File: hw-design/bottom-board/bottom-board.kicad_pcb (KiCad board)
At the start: 2 copper layers, 172 x 140.5 mm, 256 parts, among them J1 JACK_TRS_6PINS, J2 JACK_TRS_6PINS, J3 JACK_TRS_6PINS, J4 JACK_TRS_6PINS, J5 JACK_TRS_6PINS, J6 RJ45_LEDS, J7 Conn_02x50_Odd_Even, J8 Conn_02x50_Odd_Even, K1 IM06TS, K2 IM06TS, P1 USB_B, P2 USB_A, P3 DIN_5, P4 DIN_5, P5 BARREL_JACK, P6 HMI_POWER, P8 HMI_DATA, P9 SERIAL_DEBUG, Q1 2N7002, Q10 2N7002, Q12 2N7002, Q13 2N7002, Q14 BSS84, Q15 BSS84, Q2 2N7002, Q3 J112, Q4 J112, Q5 J112, Q6 J112, Q7 2N7002, Q8 2N7002, Q9 2N7002, SW1 SW_PUSH, U1 MURATA 5V, U10 RT9701, U11 6N137S, U12 ISL83491, U13 AP2120N-3.3, U2 LD1117S50TR_SOT223, U3 CS4245, U4 AT24CS08-STUM, U6 LM4562, U7 LM4562, U8 LM4562, U9 LM4811

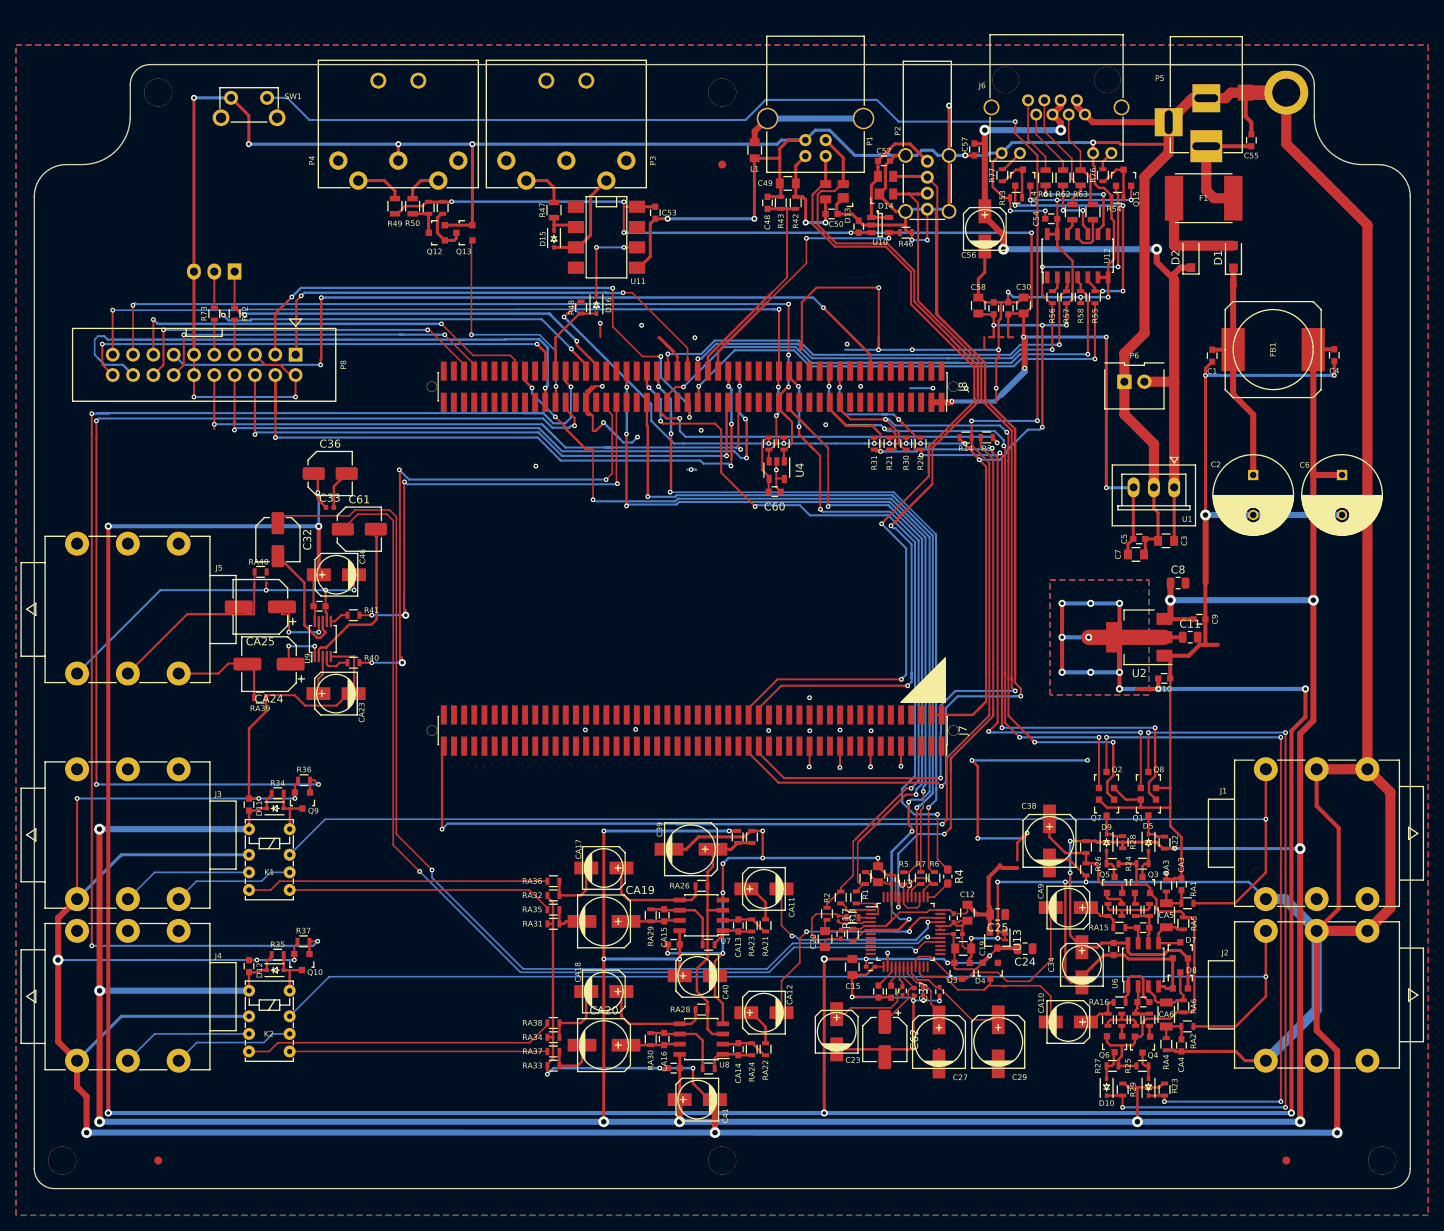
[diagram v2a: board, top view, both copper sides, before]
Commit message: Changed capacitor posistion & changed relay footprint
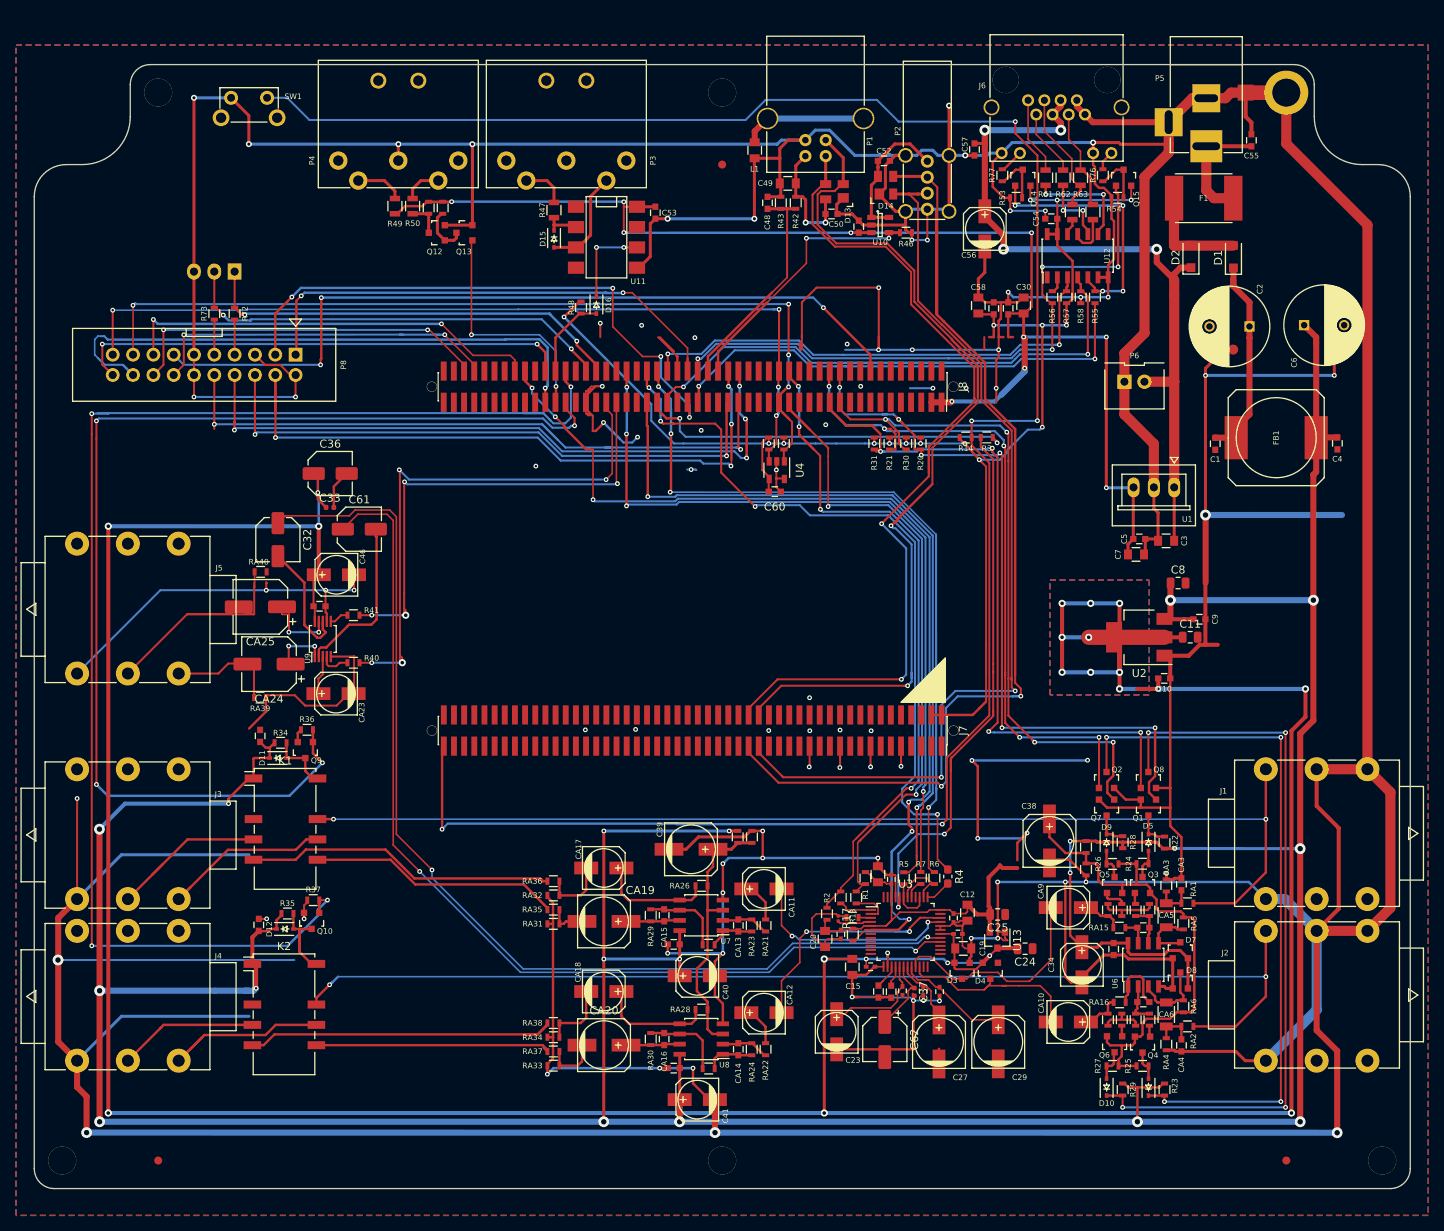
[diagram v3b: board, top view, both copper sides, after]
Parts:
- K1, K2: footprint footprints:Relay_DPDT_IMXXTS -> footprints:Relay_DPDT_Omron_G6S-2F-good_pinout
- moved C6 19.3 mm to (218.8, 52.1), turned to 0 degrees
- moved C2 18.6 mm to (212.0, 52.3), turned to 180 degrees
- moved C4 11.0 mm to (223.0, 66.9)
- moved C1 11.0 mm to (207.7, 67.0)
- moved FB1 11.0 mm to (215.3, 66.2)
- moved C44 8.70 mm to (88.3, 103.5)
- moved D11 6.31 mm to (90.6, 106.2)
- moved Q9 6.31 mm to (94.0, 105.3)
- moved R34 6.31 mm to (90.9, 104.3)
- moved R36 6.31 mm to (94.2, 102.7)
- moved K2 5.34 mm to (91.3, 138.3)
- moved D12 5.29 mm to (91.4, 127.6)
- moved C45 5.29 mm to (88.1, 127.1)
- moved Q10 5.29 mm to (94.7, 126.6)
- moved R35 5.29 mm to (91.7, 125.7)
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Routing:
- net GNDA: track 1634.4 -> 1596.5 mm, vias 88 -> 86
- net +12VA: track 519.5 -> 531.6 mm, vias 17 -> 19
- net RIGHT_AUDIO_OUTPUT_TIP: track 15.3 -> 23.2 mm
- net LEFT_AUDIO_OUTPUT_TIP: track 15.3 -> 22.6 mm
- net Net-(D12-Pad2): track 6.90 -> 12.5 mm
- net LEFT_AUDIO_INPUT: track 147.4 -> 142.1 mm, vias 1 -> 2
- net LEFT_TRUE_BYPASS: track 140.9 -> 145.5 mm
- net Net-(C1-Pad1): track 30.3 -> 26.1 mm
- net LEFT_AUDIO_OUTPUT_RING: track 16.5 -> 20.6 mm
- net RIGHT_TRUE_BYPASS: track 170.8 -> 174.6 mm
- net RIGHT_AUDIO_INPUT: track 142.9 -> 139.4 mm, vias 1 -> 2
- net Net-(K2-Pad4): track 38.9 -> 41.9 mm
- net Net-(K2-Pad5): track 32.2 -> 30.0 mm
- net Net-(K1-Pad4): track 37.8 -> 39.3 mm
- net Net-(K1-Pad5): track 33.3 -> 34.8 mm
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
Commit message: added logo's and updated gerber files
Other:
- board text added: "MOD Devices GmbH http://moddevices.com [DU-ELE-001] MOD Duo - Bottom Board Rev.: 2019.04.15"
- board text removed: "MOD Devices GmbH http://moddevices.com MOD Duo - Bottom Board Rev.: 2019.03.28"
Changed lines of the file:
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@@
   )
   (layers
-    (0 F.Cu signal)
-    (31 B.Cu signal)
+    (0 F.Cu signal hide)
+    (31 B.Cu signal hide)
     (32 B.Adhes user)
     (33 F.Adhes user)
@@
     (effects (font (size 1 1) (thickness 0.15)) (justify left mirror))
   )
-  (gr_text "MOD Devices GmbH\nhttp://moddevices.com\n\nMOD Duo - Bottom Board\nRev.: 2019.03.28" (at 208.71434 141.54912) (layer B.SilkS)
-    (effects (font (size 1.5 1.5) (thickness 0.3)) (justify left mirror))
+  (gr_text "MOD Devices GmbH\nhttp://moddevices.com\n\n[DU-ELE-001]\nMOD Duo - Bottom Board\nRev.: 2019.04.15" (at 208.71434 141.54912) (layer B.SilkS)
+    (effects (font (size 2 2) (thickness 0.4)) (justify left mirror))
   )
   (segment (start 209.931 46.49724) (end 209.93354 46.49978) (width 0.762) (layer F.Cu) (net 1) (status 30))

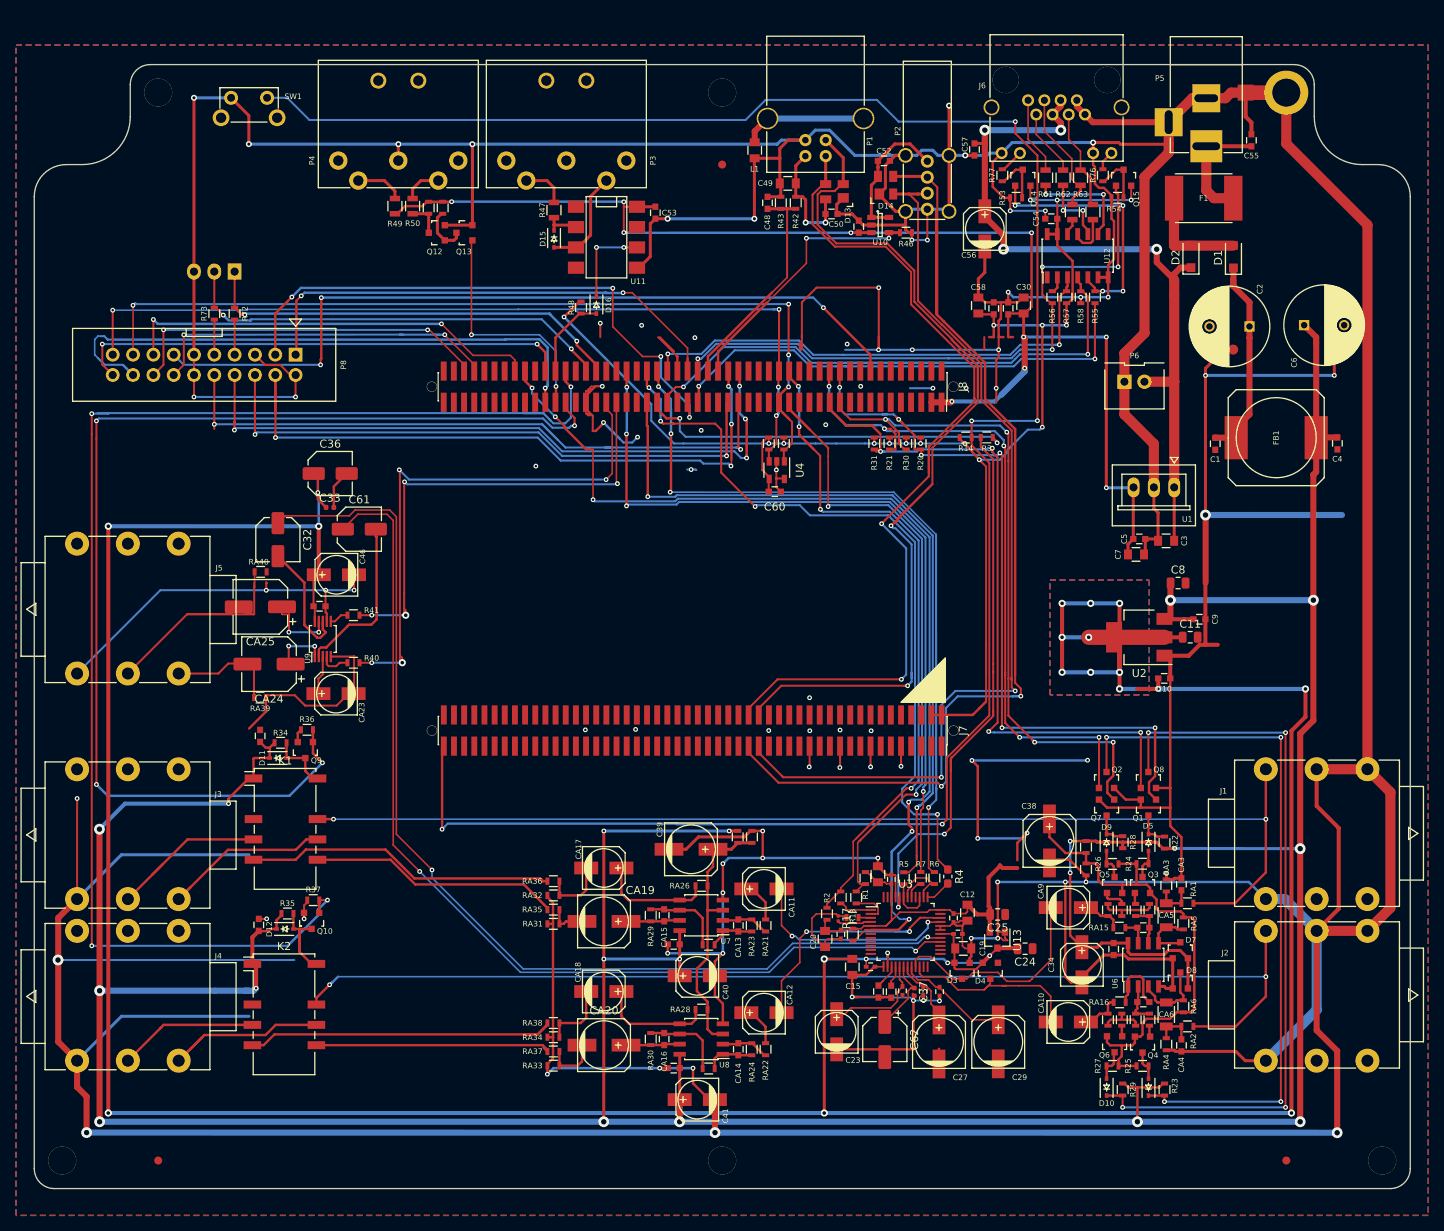
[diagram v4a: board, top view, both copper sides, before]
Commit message: updated footprints and MPN's
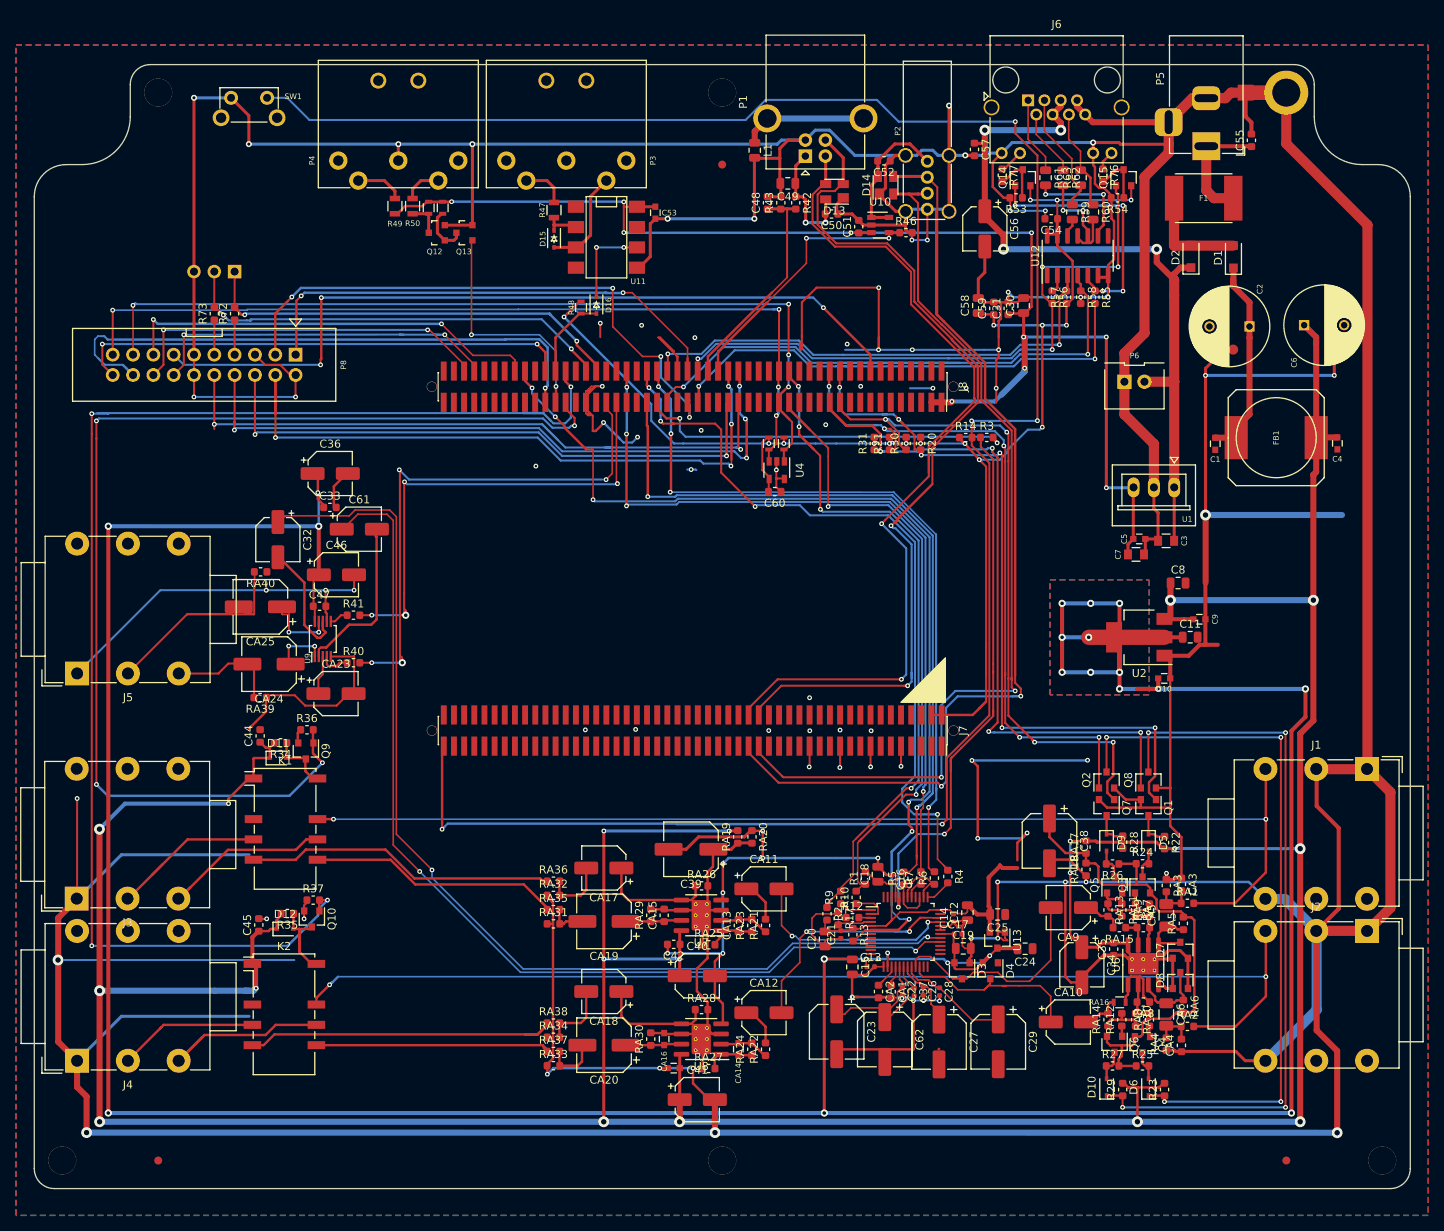
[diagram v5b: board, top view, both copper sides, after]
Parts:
- C12, C15, C18, C19, C20, C30, C49, C58, L1: footprint Capacitors_SMD:C_0805 -> Capacitor_SMD:C_0805_2012Metric
- C13, C14, C16, C17, C21, C22, C26, C28: footprint Capacitors_SMD:C_0402 -> Capacitor_SMD:C_0402_1005Metric
- C23: footprint Capacitors_SMD:c_elec_5x5.3 -> Capacitor_SMD:CP_Elec_6.3x5.3
- C27, C29, C38, C39: footprint Capacitors_SMD:c_elec_6.3x5.3 -> Capacitor_SMD:CP_Elec_6.3x5.3
- C31, C35, C42, C44, C45, C47, C48, C50, C51, C52, C54, C55, C57, C59, C60, CA1, CA13, CA15, CA2, CA3, CA4, CA7, CA8: footprint Capacitors_SMD:C_0603 -> Capacitor_SMD:C_0603_1608Metric
- C32, C36, C61: footprint Capacitor_SMD:C_Elec_5x5.4 -> Capacitor_SMD:CP_Elec_5x5.3
- C33: footprint Capacitor_SMD:C_0402_1005Metric -> Capacitor_SMD:C_0603_1608Metric
- C34, C40, C41, C46, C56, CA10, CA11, CA12, CA17, CA18, CA23, CA9: footprint Capacitors_SMD:c_elec_5x5.3 -> Capacitor_SMD:CP_Elec_5x5.3
- C62: footprint Capacitor_SMD:CP_Elec_5x5.3 -> Capacitor_SMD:CP_Elec_6.3x5.3
- CA19, CA20: footprint Capacitors_SMD:c_elec_6.3x7.7 -> Capacitor_SMD:CP_Elec_6.3x7.7
- CA5, CA6: footprint Capacitors_SMD:C_1206 -> Capacitor_SMD:C_1206_3216Metric
- D10, D11, D12, D5, D6, D9: footprint Diodes_SMD:SOD-323 -> Diode_SMD:D_SOD-323
- D13, D14: footprint Housings_SOT-23_SOT-143_TSOT-6:SOT-143 -> Package_TO_SOT_SMD:SOT-143
- D3, D4, D7, D8, Q1, Q10, Q14, Q15, Q2, Q3, Q4, Q5, Q6, Q7, Q8, Q9: footprint Housings_SOT-23_SOT-143_TSOT-6:SOT-23 -> Package_TO_SOT_SMD:SOT-23
- J1, J2, J3, J4, J5: footprint Connect:NMJ6HCD2 -> Connector_Audio:Jack_3.5mm_Neutrik_NMJ6HCD2_Horizontal
- J6: footprint Connect:RJHSE538X -> Connector_RJ:RJ45_Amphenol_RJHSE538X
- J7, J8: footprint footprints-local:Pin_Header_Straight_2x50_Pitch1.27mm_SMD -> footprints:Pin_Header_Straight_2x50_Pitch1.27mm_SMD
- P1: footprint Connect:USB_B -> Connector_USB:USB_B_OST_USB-B1HSxx_Horizontal
- P5: footprint Connect:BARREL_JACK -> Connector_BarrelJack:BarrelJack_Horizontal
- P9: footprint Pin_Headers:Pin_Header_Straight_1x03 -> Connector_PinHeader_2.54mm:PinHeader_1x03_P2.54mm_Vertical
- R1, R10, R12, R13, R14, R2, R20, R21, R22, R23, R24, R25, R26, R27, R28, R29, R3, R30, R31, R34, R35, R36, R37, R40, R41, R42, R43, R46, R5, R53, R54, R55, R56, R57, R58, R6, R7, R72, R73, R76, R77, R9, RA1, RA10, RA11, RA12, RA13, RA14, RA15, RA17, RA18, RA19, RA2, RA20, RA21, RA22, RA23, RA24, RA25, RA26, RA27, RA28, RA29, RA3, RA30, RA31, RA32, RA33, RA34, RA35, RA36, RA37, RA38, RA39, RA4, RA40, RA5, RA6, RA7, RA8, RA9: footprint Resistors_SMD:R_0603 -> Resistor_SMD:R_0603_1608Metric
- R17: footprint Resistor_SMD:R_0201_0603Metric -> Resistor_SMD:R_0603_1608Metric
- R4: footprint Resistor_SMD:R_0603_1608Metric_Pad1.05x0.95mm_HandSolder -> Resistor_SMD:R_0603_1608Metric
- R59, R60, R61, R62, R63: footprint Resistors_SMD:R_0805 -> Resistor_SMD:R_0805_2012Metric
- U10: value RT9701 -> RT9742MNGJ5; footprint Housings_SOT-23_SOT-143_TSOT-6:SOT-23-5 -> Package_TO_SOT_SMD:SOT-23-5
- U12: footprint Housings_SOIC:SOIC-14_3.9x8.7mm_Pitch1.27mm -> Package_SO:SOIC-14_3.9x8.7mm_P1.27mm
- U6, U7, U8: footprint Housings_SOIC:SOIC-8_3.9x4.9mm_Pitch1.27mm -> Package_SO:SOIC-8-1EP_3.9x4.9mm_P1.27mm_EP2.41x3.81mm_ThermalVias
- moved J1 12.7 mm to (214.0, 107.6), turned to 0 degrees
- moved J2 12.7 mm to (214.0, 127.9), turned to 0 degrees
- moved J5 12.7 mm to (78.1, 95.7), turned to 180 degrees
- moved J4 12.7 mm to (78.1, 144.1), turned to 180 degrees
- moved J3 12.7 mm to (78.1, 123.8), turned to 180 degrees
- moved Q10 0.24 mm to (94.8, 126.4), turned to 270 degrees
- moved Q9 0.12 mm to (94.0, 105.4), turned to 270 degrees
- turned C23 to 270 degrees
- turned C27 to 270 degrees
- turned C29 to 270 degrees
- turned C34 to 270 degrees
- turned C38 to 270 degrees
- turned C39 to 180 degrees
- turned C40 to 0 degrees
- turned C41 to 0 degrees
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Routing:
- net +5V: track 172.7 -> 169.3 mm
- net +3V3: track 192.7 -> 190.6 mm
- net GNDA: track 1596.5 -> 1594.6 mm, vias 86 -> 87
